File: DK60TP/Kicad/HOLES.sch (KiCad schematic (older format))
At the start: 7 parts

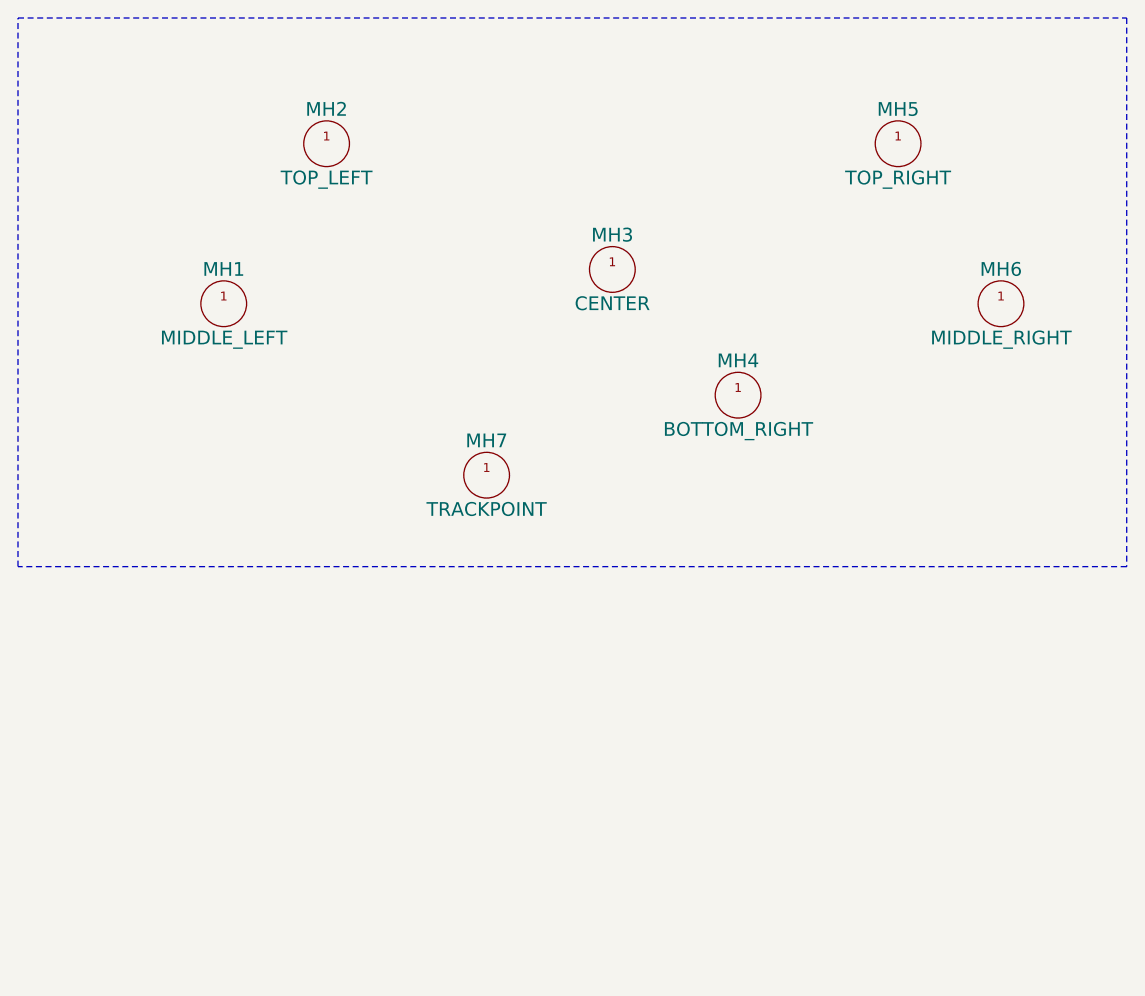
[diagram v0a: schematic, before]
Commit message: - DK60TP: Added RGB underglow
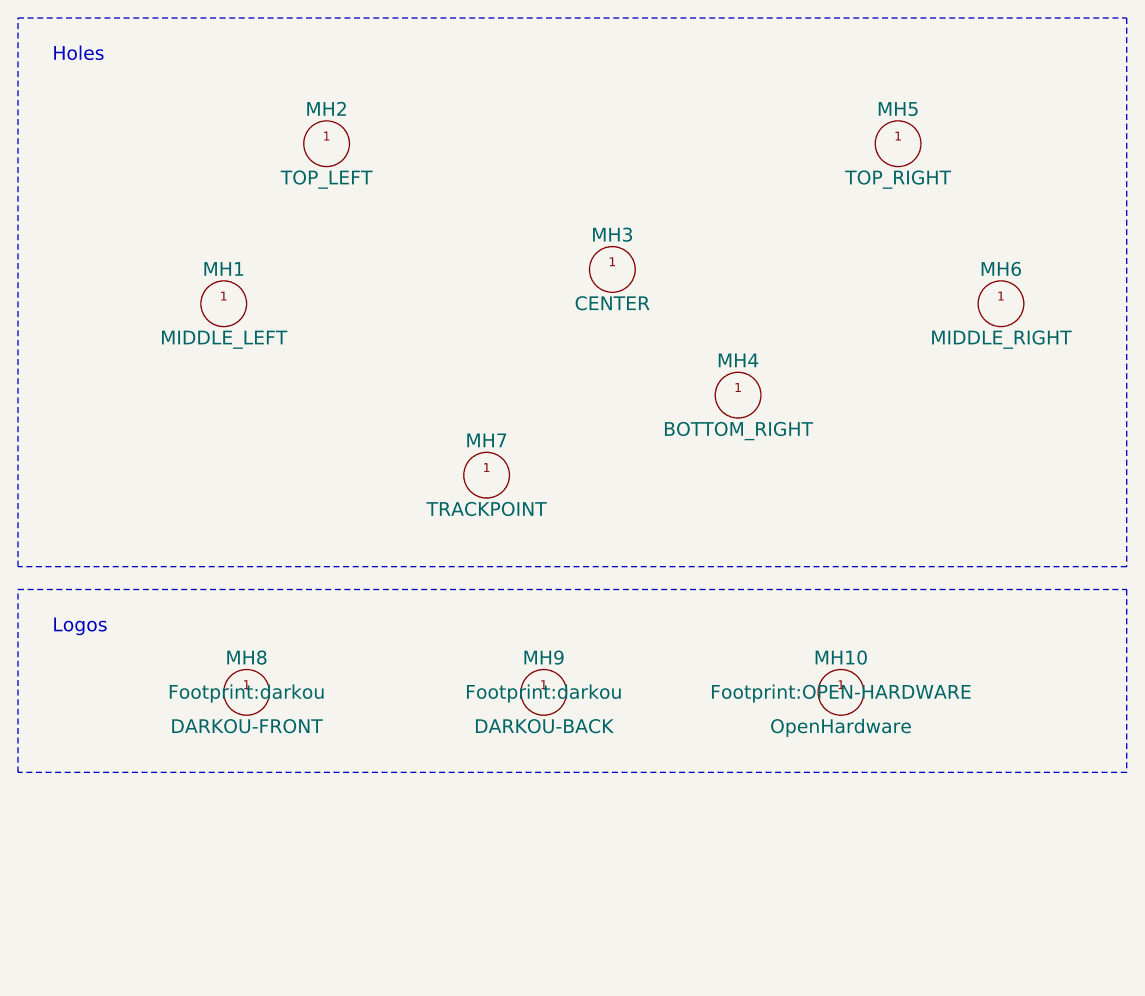
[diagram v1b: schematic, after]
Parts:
- added MH10: OpenHardware, Footprint:OPEN-HARDWARE, symbol MOUNT_HOLE
- added MH8: DARKOU-FRONT, Footprint:darkou, symbol MOUNT_HOLE
- added MH9: DARKOU-BACK, Footprint:darkou, symbol MOUNT_HOLE
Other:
- note added: "Holes"
- note added: "Logos"
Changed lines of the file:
@@
 Wire Notes Line
 	650  3000 650  600
+Text Notes 800  800  0    60   ~ 0
+Holes
+$Comp
+L MOUNT_HOLE MH8
+U 1 1 59355090
+P 1650 3550
+F 0 "MH8" H 1650 3700 60  0000 C CNN
+F 1 "DARKOU-FRONT" H 1650 3400 60  0000 C CNN
+F 2 "Footprint:darkou" H 1650 3550 60  0000 C CNN
+F 3 "" H 1650 3550 60  0000 C CNN
+	1    1650 3550
+	1    0    0    -1
+$EndComp
+$Comp
+L MOUNT_HOLE MH9
+U 1 1 59355198
+P 2950 3550
+F 0 "MH9" H 2950 3700 60  0000 C CNN
+F 1 "DARKOU-BACK" H 2950 3400 60  0000 C CNN
+F 2 "Footprint:darkou" H 2950 3550 60  0000 C CNN
+F 3 "" H 2950 3550 60  0000 C CNN
+	1    2950 3550
+	1    0    0    -1
+$EndComp
+$Comp
+L MOUNT_HOLE MH10
+U 1 1 5935520E
+P 4250 3550
+F 0 "MH10" H 4250 3700 60  0000 C CNN
+F 1 "OpenHardware" H 4250 3400 60  0000 C CNN
+F 2 "Footprint:OPEN-HARDWARE" H 4250 3550 60  0000 C CNN
+F 3 "" H 4250 3550 60  0000 C CNN
+	1    4250 3550
+	1    0    0    -1
+$EndComp
+Wire Notes Line
+	650  3100 5500 3100
+Wire Notes Line
+	5500 3100 5500 3900
+Wire Notes Line
+	5500 3900 650  3900
+Wire Notes Line
+	650  3900 650  3100
+Text Notes 800  3300 0    60   ~ 0
+Logos
 $EndSCHEMATC

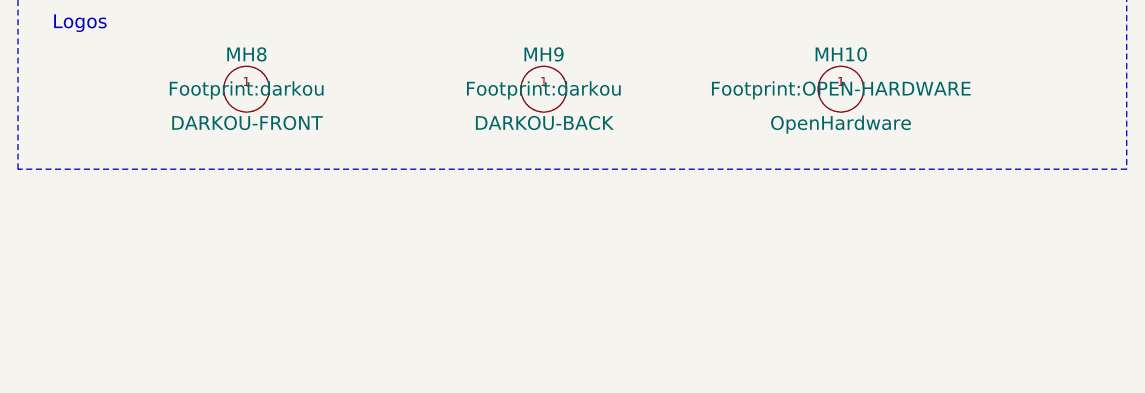
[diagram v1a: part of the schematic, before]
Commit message: - DK60TP: Added holes for Mouse button's PCB
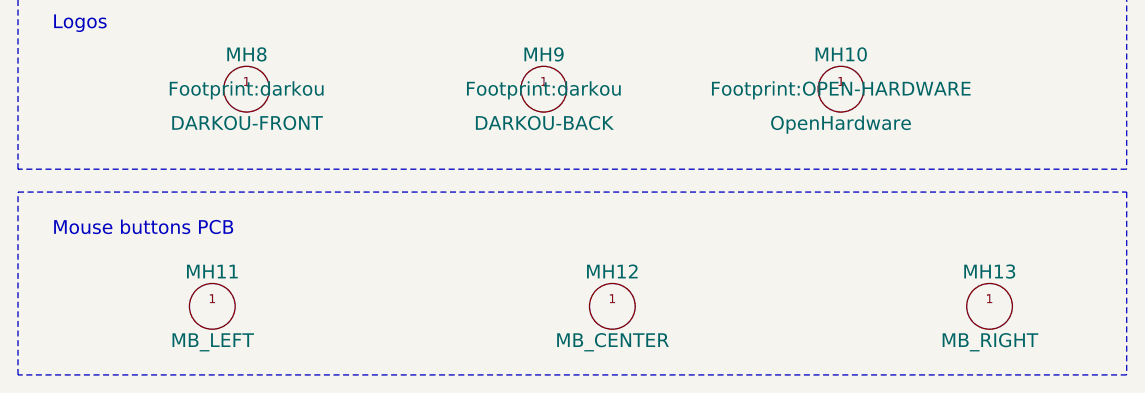
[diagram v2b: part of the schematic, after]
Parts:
- added MH11: MB_LEFT, Footprint:Poker_oval_hole, symbol MOUNT_HOLE
- added MH12: MB_CENTER, Footprint:Poker_oval_hole, symbol MOUNT_HOLE
- added MH13: MB_RIGHT, Footprint:Poker_oval_hole, symbol MOUNT_HOLE
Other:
- note added: "Mouse buttons PCB"
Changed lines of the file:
@@
 LIBS:keyboard_parts
 LIBS:mkl27z256vfm4
-LIBS:TS65
 LIBS:DK60TP-cache
 EELAYER 25 0
@@
 Text Notes 800  3300 0    60   ~ 0
 Logos
+Wire Notes Line
+	650  4000 5500 4000
+Wire Notes Line
+	5500 4000 5500 4800
+Wire Notes Line
+	5500 4800 650  4800
+Wire Notes Line
+	650  4800 650  4000
+Text Notes 800  4200 0    60   ~ 0
+Mouse buttons PCB
+$Comp
+L MOUNT_HOLE MH11
+U 1 1 593CB643
+P 1500 4500
+F 0 "MH11" H 1500 4650 60  0000 C CNN
+F 1 "MB_LEFT" H 1500 4350 60  0000 C CNN
+F 2 "Footprint:Poker_oval_hole" H 1500 4500 60  0001 C CNN
+F 3 "" H 1500 4500 60  0000 C CNN
+	1    1500 4500
+	1    0    0    -1
+$EndComp
+$Comp
+L MOUNT_HOLE MH13
+U 1 1 593CB6EE
+P 4900 4500
+F 0 "MH13" H 4900 4650 60  0000 C CNN
+F 1 "MB_RIGHT" H 4900 4350 60  0000 C CNN
+F 2 "Footprint:Poker_oval_hole" H 4900 4500 60  0001 C CNN
+F 3 "" H 4900 4500 60  0000 C CNN
+	1    4900 4500
+	1    0    0    -1
+$EndComp
+$Comp
+L MOUNT_HOLE MH12
+U 1 1 593CB794
+P 3250 4500
+F 0 "MH12" H 3250 4650 60  0000 C CNN
+F 1 "MB_CENTER" H 3250 4350 60  0000 C CNN
+F 2 "Footprint:Poker_oval_hole" H 3250 4500 60  0001 C CNN
+F 3 "" H 3250 4500 60  0000 C CNN
+	1    3250 4500
+	1    0    0    -1
+$EndComp
 $EndSCHEMATC
